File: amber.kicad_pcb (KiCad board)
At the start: 2 copper layers, 118.8 x 112.3 mm, 46 parts, among them J1 MJ-4PP-9

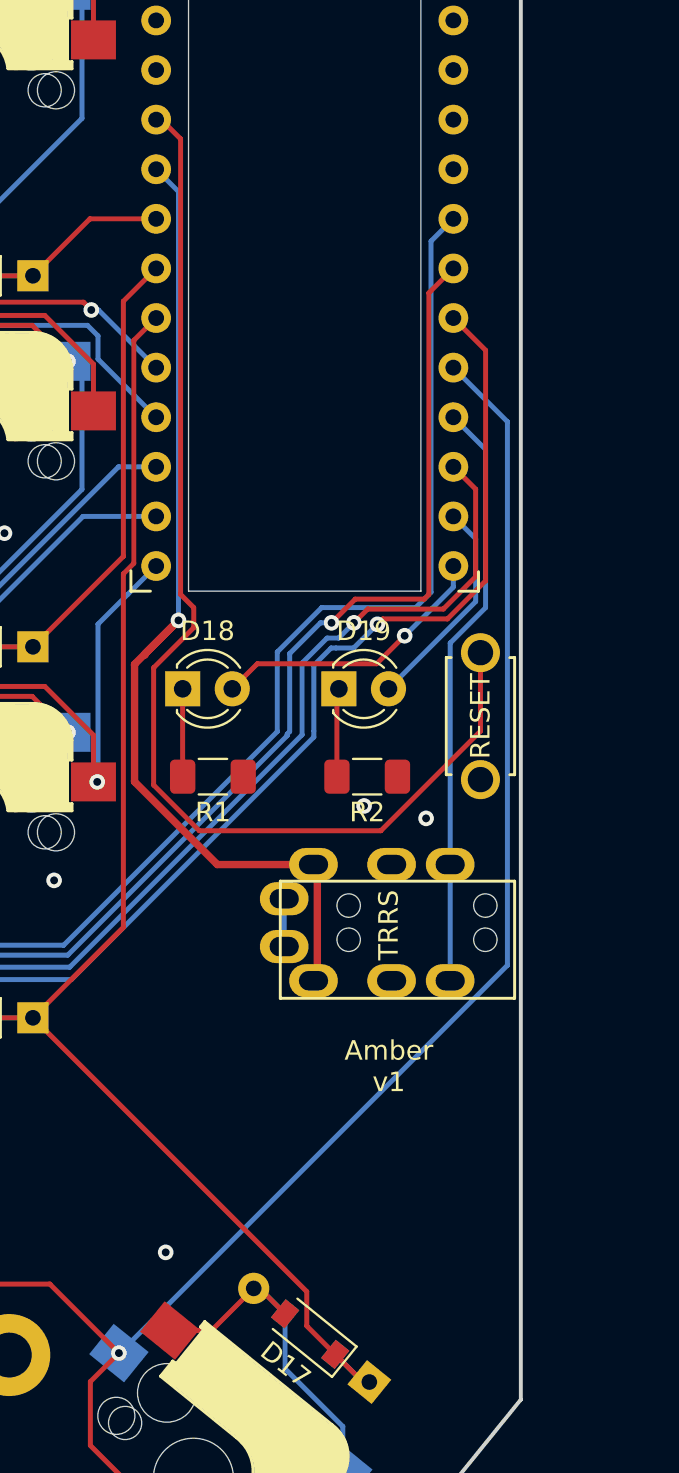
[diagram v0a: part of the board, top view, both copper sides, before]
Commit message: Use a mid-mount TRRS jack SJ 43504
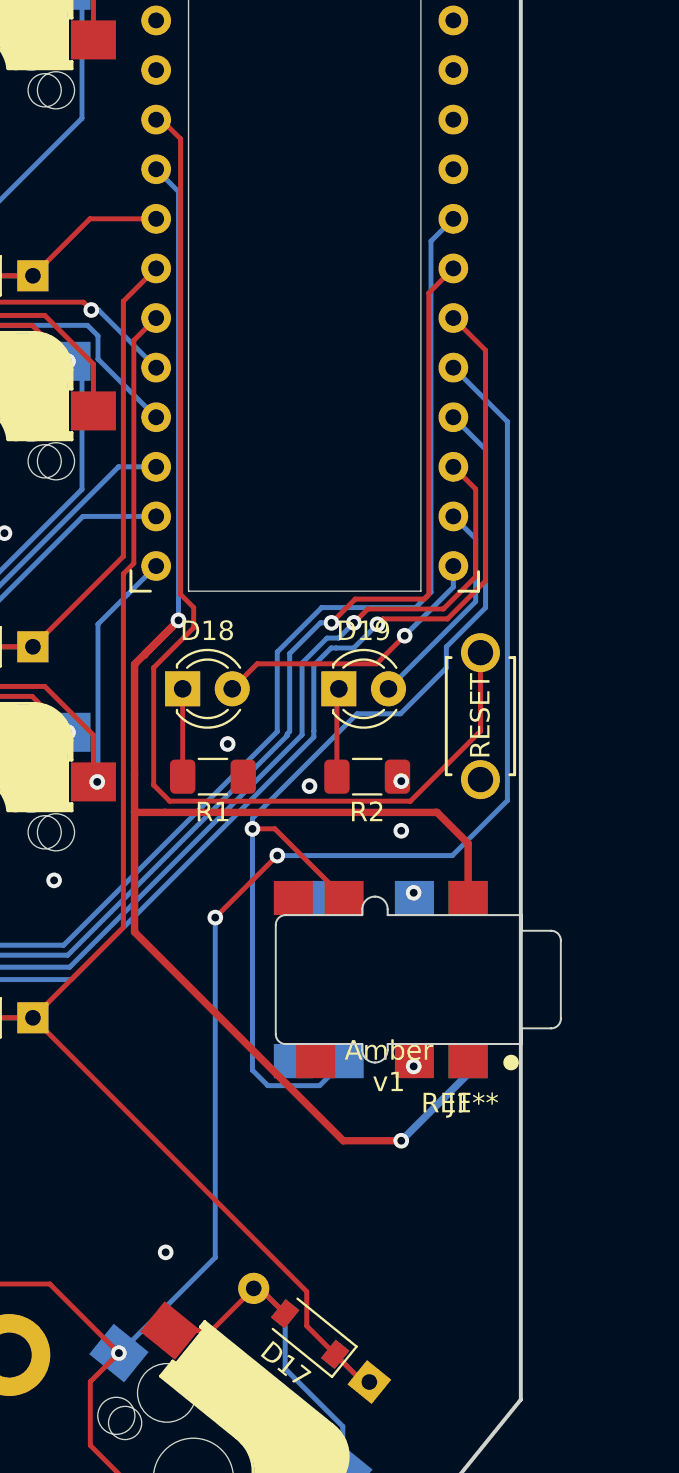
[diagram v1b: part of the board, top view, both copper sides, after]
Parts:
- J1: value MJ-4PP-9 -> SJ-43504-SMT-TR; footprint kbd:MJ-4PP-9 -> amber:CUI_SJ-43504-SMT-TR-dual
- moved J1 6.27 mm to (99.6, 8.89), turned to 180 degrees
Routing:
- net VCC: track 52.3 -> 89.4 mm, vias 1 -> 2
- net Serial: track 30.3 -> 52.6 mm, vias 0 -> 1
- net CT: track 112.2 -> 117.4 mm, vias 2 -> 4
- net Net-(J1-PadA): track 2.45 -> 0.00 mm
- net RST: track 59.7 -> 58.5 mm
- net GND: vias 10 -> 14

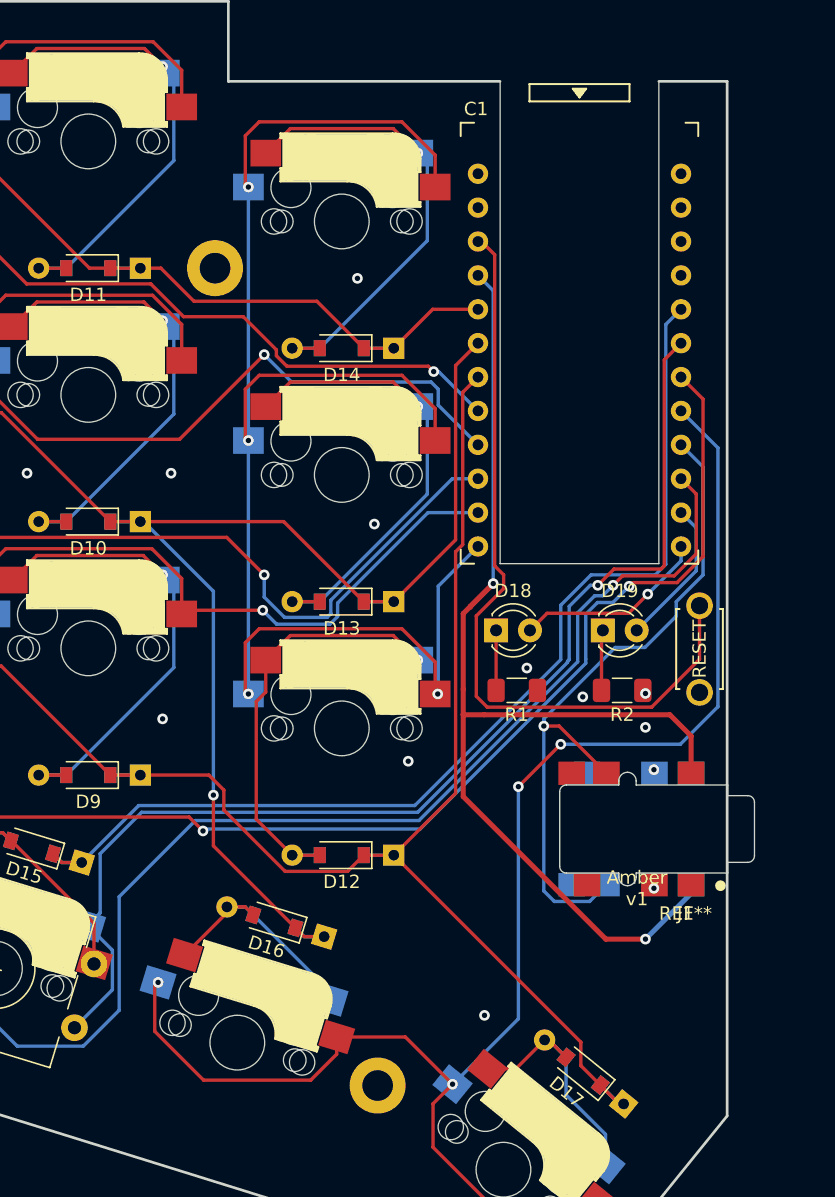
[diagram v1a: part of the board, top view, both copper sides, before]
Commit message: Widen the promicro pad holes
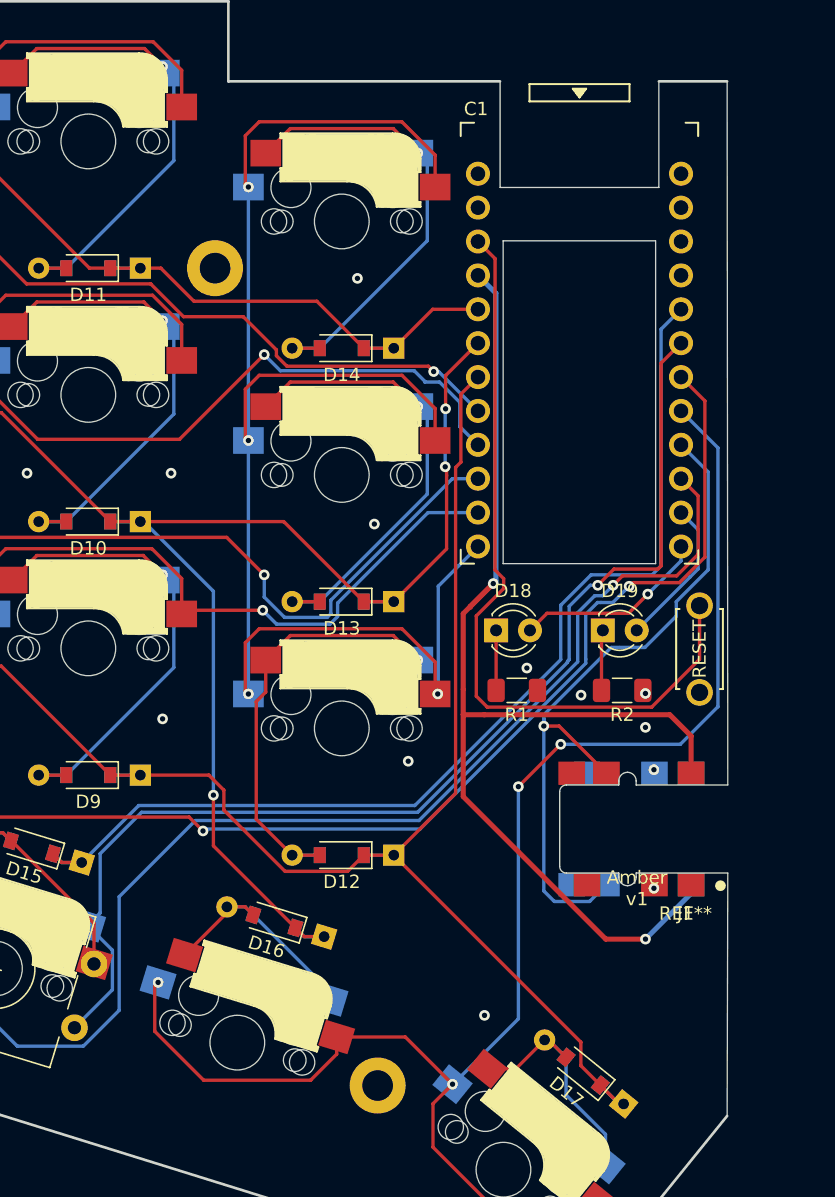
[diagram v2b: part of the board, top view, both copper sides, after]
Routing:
- net Serial: track 52.6 -> 53.6 mm
- net RM: vias 1 -> 3
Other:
- board size 118.8 x 112.3 mm -> 118.9 x 112.3 mm

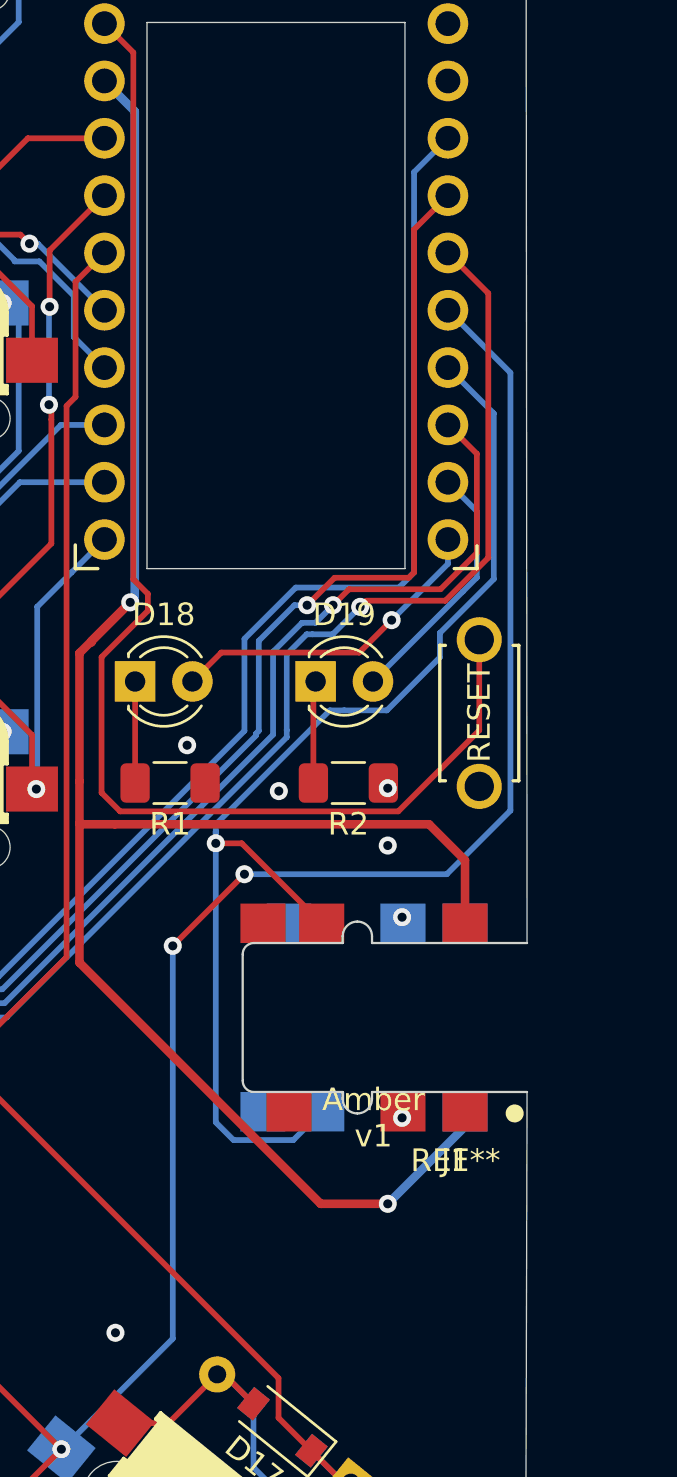
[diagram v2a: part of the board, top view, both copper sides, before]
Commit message: Move serial to D1
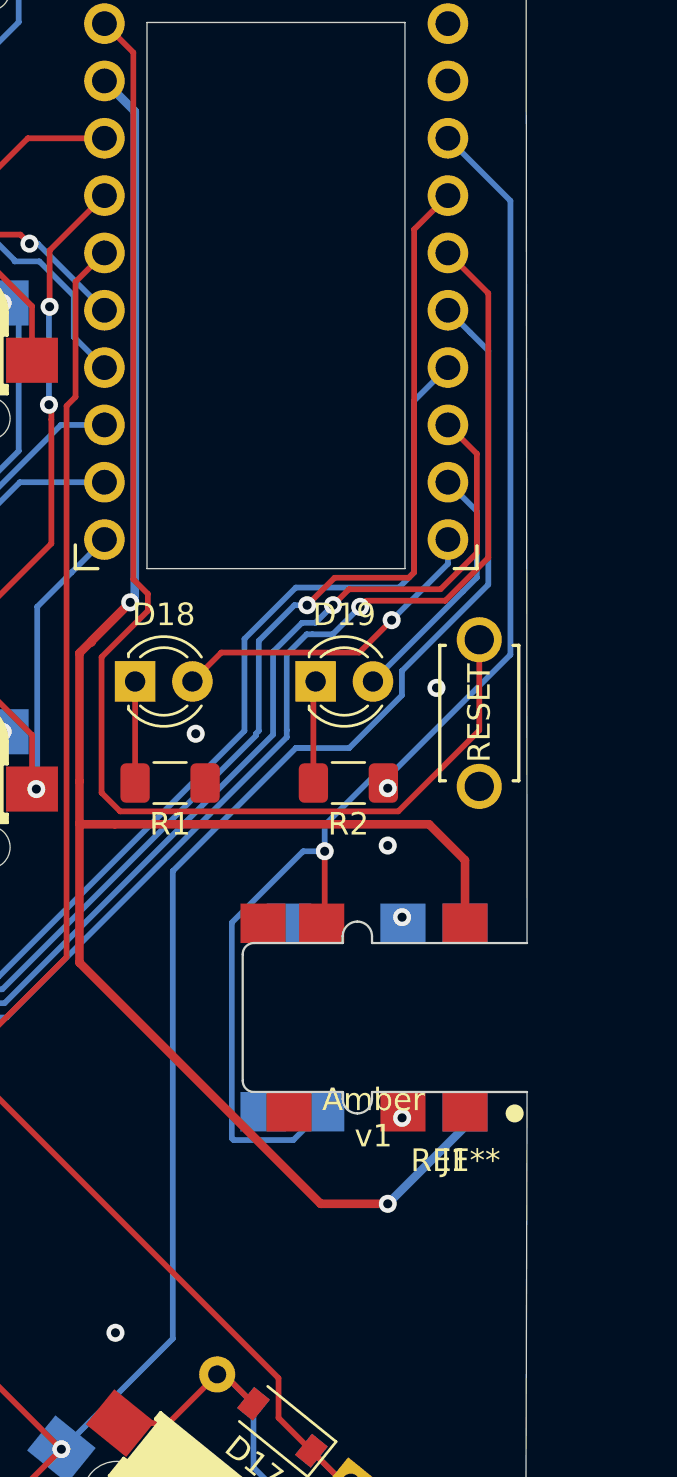
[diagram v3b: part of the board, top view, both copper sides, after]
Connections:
- C1 pad 5: RE -> Serial
- C1 pad 9: Serial -> RE
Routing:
- net RE: track 79.7 -> 69.4 mm
- net Serial: track 53.6 -> 59.3 mm
- net CT: track 117.4 -> 113.4 mm, vias 4 -> 2

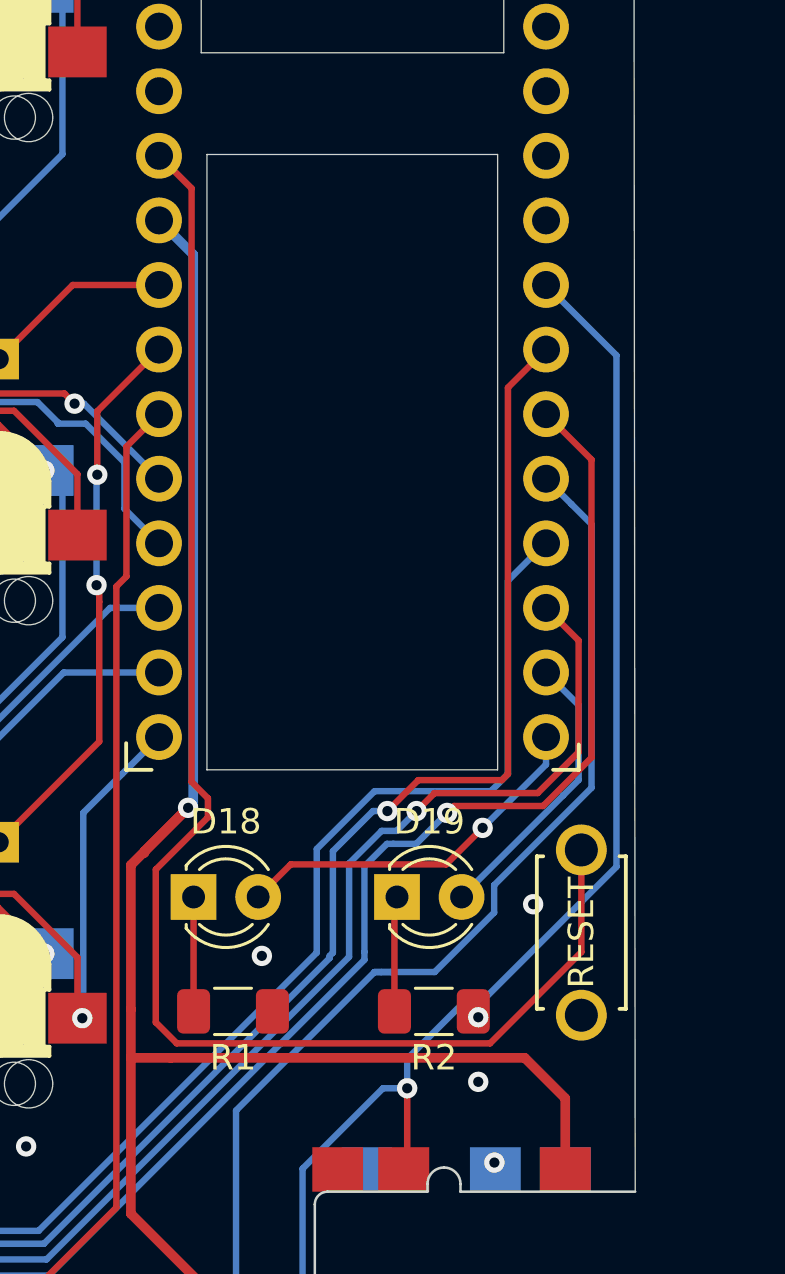
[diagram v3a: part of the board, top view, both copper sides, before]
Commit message: Add magnets, use side switch for reset
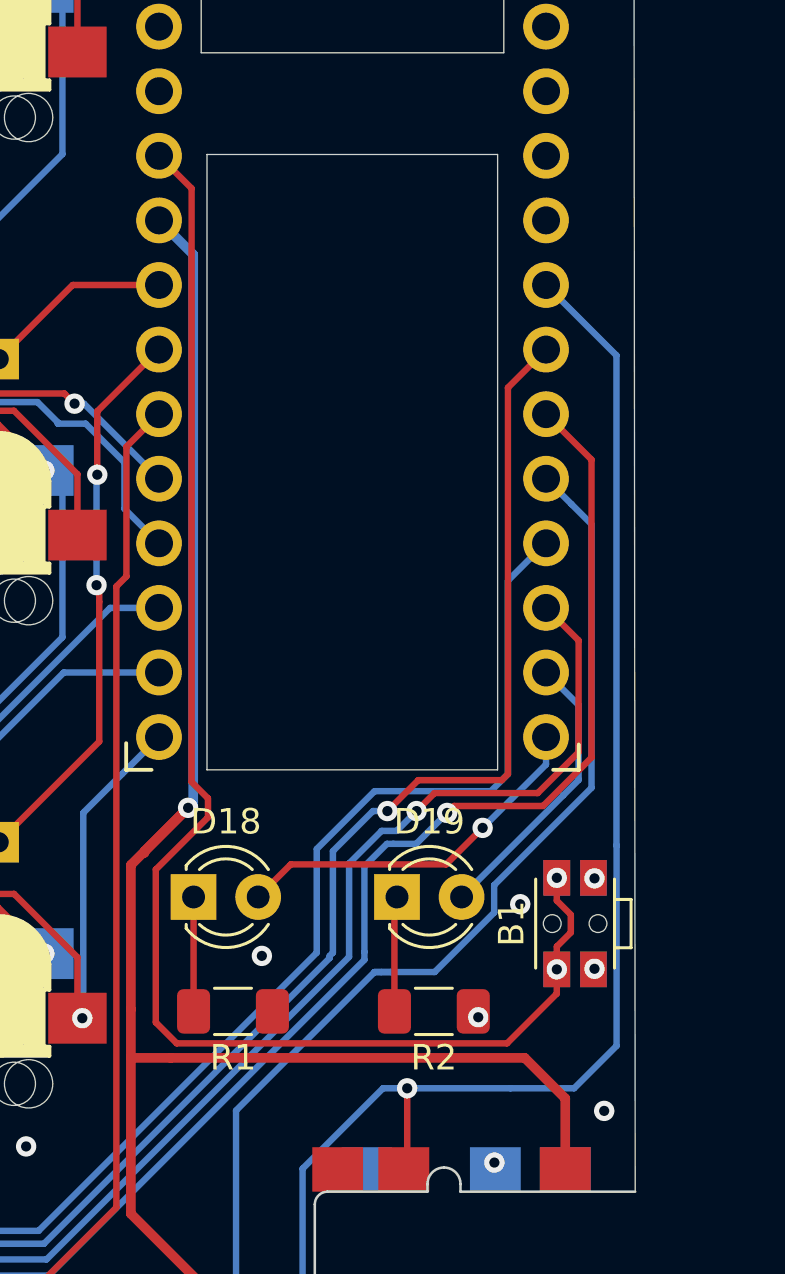
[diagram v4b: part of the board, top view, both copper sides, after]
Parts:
- B1: footprint kbd:ResetSW -> amber:SW_SPST_EVQP7C
- moved B1 0.43 mm to (103.5, -4.95)
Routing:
- net Serial: track 59.3 -> 62.8 mm
- net RST: track 58.3 -> 57.7 mm, vias 0 -> 2
- net GND: vias 14 -> 16

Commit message: Prettify the ground vias
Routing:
- net GND: vias 16 -> 15
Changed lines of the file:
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@@
     (thickness 1.6)
     (drawings 29)
-    (tracks 629)
+    (tracks 628)
     (zones 0)
     (modules 46)
@@
   (gr_line (start -13.031138 -28.472608) (end 9.432076 -30.4) (layer Edge.Cuts) (width 0.2))
   (gr_line (start -13.031138 -28.472608) (end -9.544909 11.375179) (layer Edge.Cuts) (width 0.2))
-  (via (at 104.267 -6.731) (size 0.8) (drill 0.4) (layers F.Cu B.Cu) (net 1))
-  (via (at 104.267 -3.175) (size 0.8) (drill 0.4) (layers F.Cu B.Cu) (net 1))
+  (via (at 103.886 -8.509) (size 0.8) (drill 0.4) (layers F.Cu B.Cu) (net 1))
+  (via (at 103.886 -0.762) (size 0.8) (drill 0.4) (layers F.Cu B.Cu) (net 1))
   (via (at 100.33 13.335) (size 0.8) (drill 0.4) (layers F.Cu B.Cu) (net 1))
-  (via (at 99.695 -1.27) (size 0.8) (drill 0.4) (layers F.Cu B.Cu) (net 1))
+  (via (at 101.092 -3.048) (size 0.8) (drill 0.4) (layers F.Cu B.Cu) (net 1))
   (via (at 100.33 4.445) (size 0.8) (drill 0.4) (layers F.Cu B.Cu) (net 1))
   (via (at 87.63 22.86) (size 0.8) (drill 0.4) (layers F.Cu B.Cu) (net 1))
@@
   (via (at 46.355 -29.845) (size 0.8) (drill 0.4) (layers F.Cu B.Cu) (net 1))
   (via (at 91.186 -3.683) (size 0.8) (drill 0.4) (layers F.Cu B.Cu) (net 1))
-  (via (at 101.346 -5.715) (size 0.8) (drill 0.4) (layers F.Cu B.Cu) (net 1))
   (via (at 104.648 2.413) (size 0.8) (drill 0.4) (layers F.Cu B.Cu) (net 1))
   (segment (start 88.422401 -33.866999) (end 87.1414 -35.148) (width 0.254) (layer F.Cu) (net 2))

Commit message: Update silkscreen
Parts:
- S1, S10, S11, S12, S13, S14, S16, S17, S2, S3, S4, S5, S6, S7, S8, S9: footprint kbd:CherryMX_MidHeight_Hotswap -> amber:CherryMX_MidHeight_Hotswap
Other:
- board text added: "Amber v2"
- board text removed: "Amber v1"
